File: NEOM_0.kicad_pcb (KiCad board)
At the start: 2 copper layers, 28 x 24 mm, 20 parts, among them U1 LM3940, U2 7_Pins_Header_PA0_PA6, U3 Reset Button, U4 STM32F070F6P6, U6 7_Pins_Header_PA7_PA14, U7 TPD4S012DRYR, U8 16Mhz, U9 USB_Micro_B

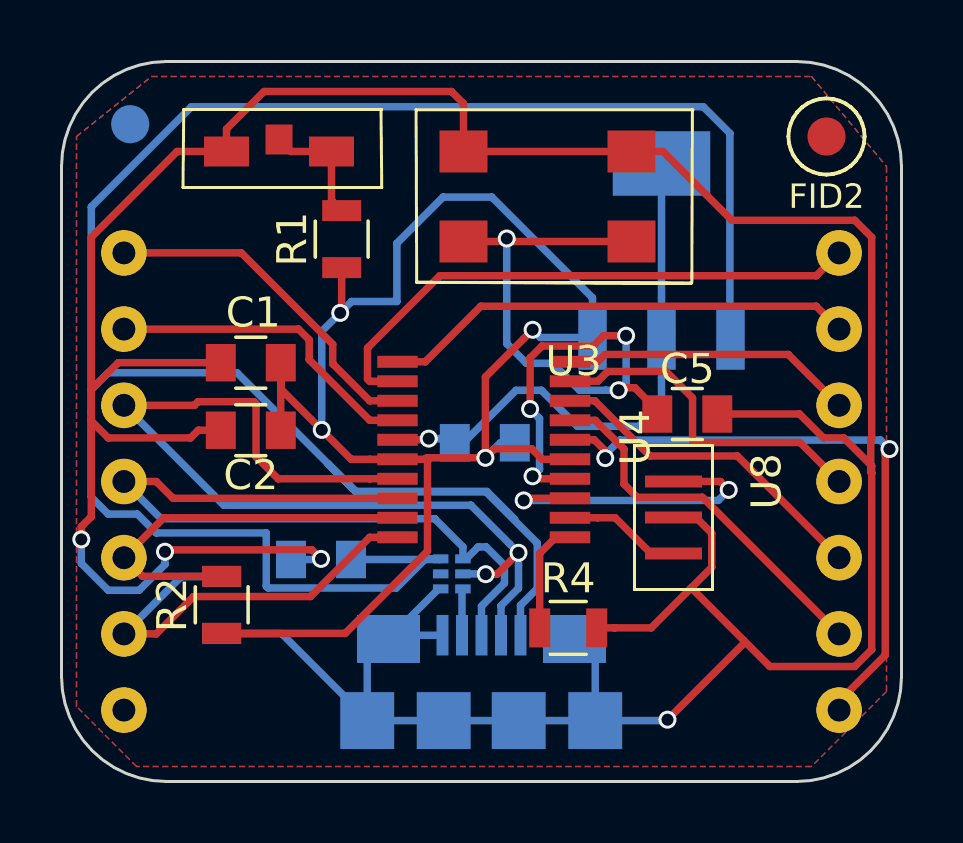
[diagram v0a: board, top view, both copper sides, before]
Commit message: Updated the PCB unconnected GND pad..
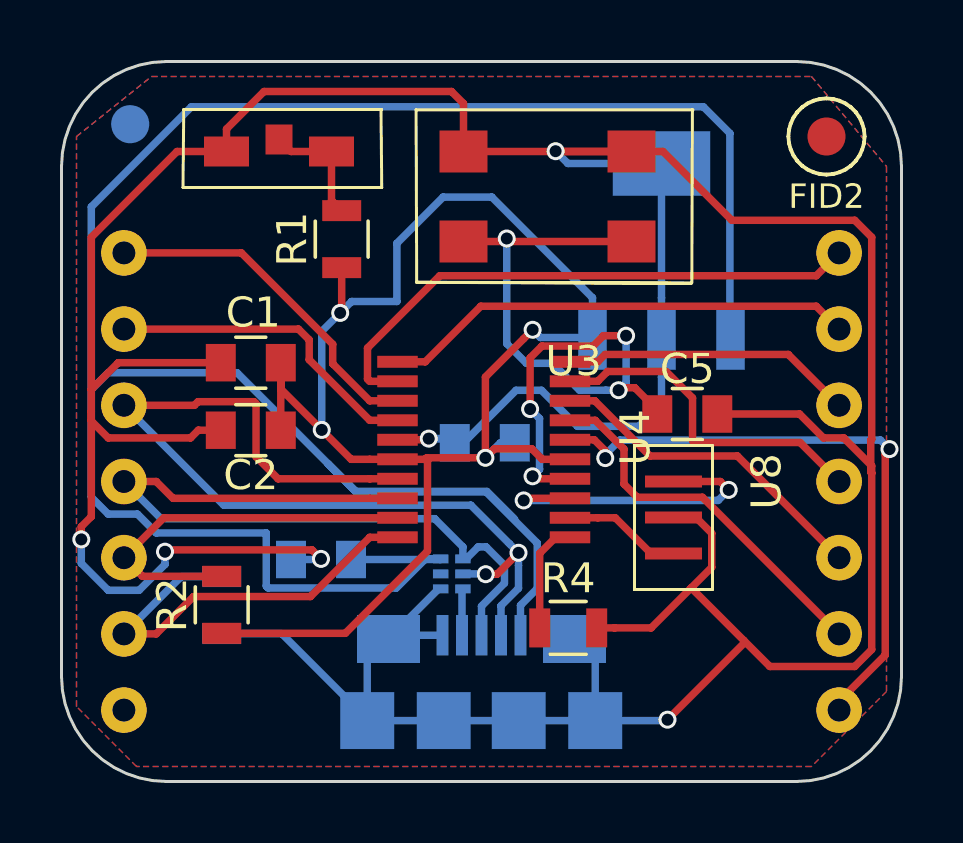
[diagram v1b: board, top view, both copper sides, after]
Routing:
- net GND: track 146.2 -> 152.5 mm, vias 5 -> 6
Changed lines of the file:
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@@
   (general
     (links 59)
-    (no_connects 1)
+    (no_connects 0)
     (area 105.875 87.31474 141.975 116.015)
     (thickness 1.6)
     (drawings 9)
-    (tracks 319)
+    (tracks 324)
     (zones 0)
     (modules 20)
@@
     (visible_elements FFFFFF7F)
     (pcbplotparams
-      (layerselection 0x00030_80000001)
+      (layerselection 0x010fc_80000001)
       (usegerberextensions false)
       (excludeedgelayer true)
@@
       (outputformat 1)
       (mirror false)
-      (drillshape 1)
+      (drillshape 0)
       (scaleselection 1)
-      (outputdirectory ""))
+      (outputdirectory Gerbers/))
   )
   (net 0 "")
@@
   (segment (start 117.31 99.04) (end 117.31 99.915) (width 0.25) (layer F.Cu) (net 1))
   (segment (start 120.275 102.26) (end 121.2 102.26) (width 0.25) (layer F.Cu) (net 1))
+  (segment (start 130 92.4) (end 126.88 92.4) (width 0.25) (layer B.Cu) (net 2))
+  (segment (start 126.47 92) (end 129 92) (width 0.25) (layer F.Cu) (net 2))
+  (segment (start 126.47 91.99) (end 126.47 92) (width 0.25) (layer F.Cu) (net 2))
+  (via (at 126.47 91.99) (size 0.6) (drill 0.4) (layers F.Cu B.Cu) (net 2))
+  (segment (start 126.88 92.4) (end 126.47 91.99) (width 0.25) (layer B.Cu) (net 2))
   (segment (start 127.200267 101.159988) (end 129.253602 101.159988) (width 0.25) (layer B.Cu) (net 2))
   (segment (start 130 100.41359) (end 130 99.525) (width 0.25) (layer B.Cu) (net 2))
@@
   (segment (start 123.539998 101.57) (end 125.1499 99.960098) (width 0.25) (layer B.Cu) (net 2))
   (segment (start 136.974998 101.619998) (end 136.974998 102.687997) (width 0.25) (layer F.Cu) (net 2))
+  (segment (start 132.342999 94.292999) (end 136.441761 94.292999) (width 0.25) (layer F.Cu) (net 2))
+  (segment (start 137.007001 94.858239) (end 137.007001 101.587995) (width 0.25) (layer F.Cu) (net 2))
+  (segment (start 129 92) (end 130.05 92) (width 0.25) (layer F.Cu) (net 2))
+  (segment (start 130.05 92) (end 132.342999 94.292999) (width 0.25) (layer F.Cu) (net 2))
+  (segment (start 136.974998 102.687997) (end 137.007001 102.72) (width 0.25) (layer F.Cu) (net 2))
+  (segment (start 136.441761 94.292999) (end 137.007001 94.858239) (width 0.25) (layer F.Cu) (net 2))
   (segment (start 137.007001 101.587995) (end 136.974998 101.619998) (width 0.25) (layer F.Cu) (net 2))
-  (segment (start 136.441761 94.292999) (end 137.007001 94.858239) (width 0.25) (layer F.Cu) (net 2))
-  (segment (start 136.974998 102.687997) (end 137.007001 102.72) (width 0.25) (layer F.Cu) (net 2))
-  (segment (start 130.05 92) (end 132.342999 94.292999) (width 0.25) (layer F.Cu) (net 2))
-  (segment (start 129 92) (end 130.05 92) (width 0.25) (layer F.Cu) (net 2))
-  (segment (start 137.007001 94.858239) (end 137.007001 101.587995) (width 0.25) (layer F.Cu) (net 2))
-  (segment (start 132.342999 94.292999) (end 136.441761 94.292999) (width 0.25) (layer F.Cu) (net 2))
   (segment (start 110.992999 99.938239) (end 110.992999 100.65) (width 0.25) (layer F.Cu) (net 2))
   (segment (start 110.992999 100.65) (end 110.992999 100.981761) (width 0.25) (layer F.Cu) (net 2))

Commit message: Added BAT pin for external battery board..
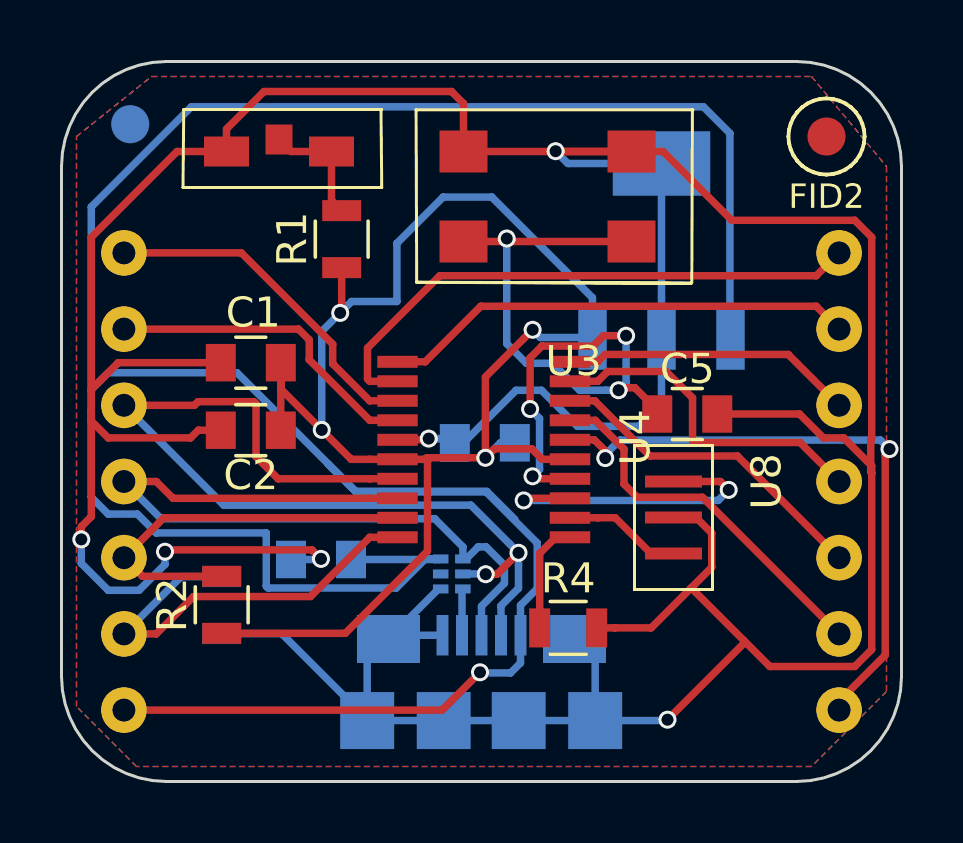
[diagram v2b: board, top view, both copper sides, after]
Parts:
- D1: value PWR -> LED
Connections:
- U6 pad 7: Net-(U6-Pad7) -> /VBUS
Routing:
- net /VBUS: track 84.6 -> 99.4 mm, vias 0 -> 1

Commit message: Updated PCB with logo..
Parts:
- added G***: LOGO, Graphics:logo, B.Cu at (116.2, 95.7)

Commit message: Updated PCB with logo..
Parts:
- moved G*** 2.29 mm to (116.2, 98.0)
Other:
- board text added: "Proudly Designed in"
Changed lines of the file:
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@@
 (kicad_pcb (version 4) (host pcbnew 4.0.2-stable)
   (general
-    (links 0)
+    (links 60)
     (no_connects 0)
-    (area 105.875 87.31474 141.975 116.015)
+    (area 109.949999 88.949999 138.050001 113.050001)
     (thickness 1.6)
-    (drawings 9)
+    (drawings 10)
     (tracks 331)
     (zones 0)
@@
   )
   (module Graphics:logo (layer B.Cu)
-    (at 116.22 95.69 180)
+    (at 116.16 97.98 180)
     (fp_text reference G*** (at 0 0 180) (layer B.SilkS) hide
       (effects (font (thickness 0.3)) (justify mirror))
@@
       (xy -0.00539 1.56421) (xy 0 1.564641) (xy 0.02429 1.548197)) (layer B.SilkS) (width 0.01))
   )
-  (gr_text "NEOM 0" (at 119.5 92) (layer B.SilkS)
+  (gr_text "Proudly\nDesigned in" (at 119.42 94.52) (layer B.SilkS)
+    (effects (font (size 1 1) (thickness 0.1)) (justify mirror))
+  )
+  (gr_text "NEOM 0\n" (at 119.5 92) (layer B.SilkS)
     (effects (font (size 1.5 1.5) (thickness 0.3)) (justify mirror))
   )

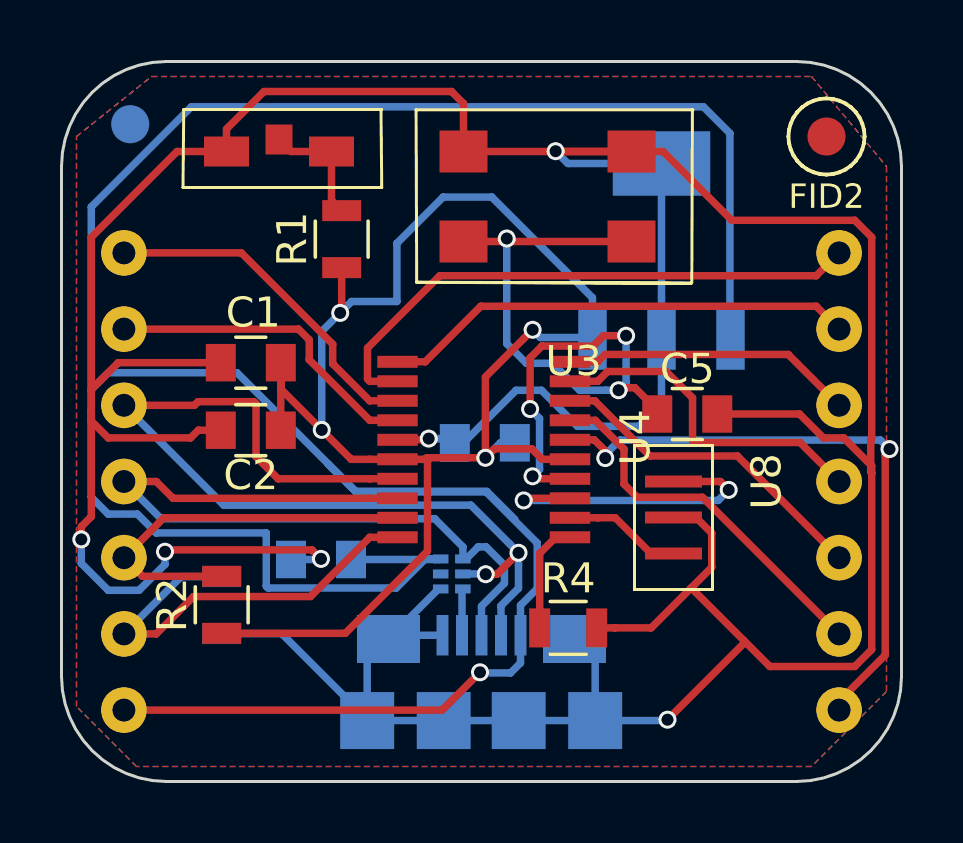
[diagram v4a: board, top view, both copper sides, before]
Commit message: Updated PCB with deminsion and Fab layer..
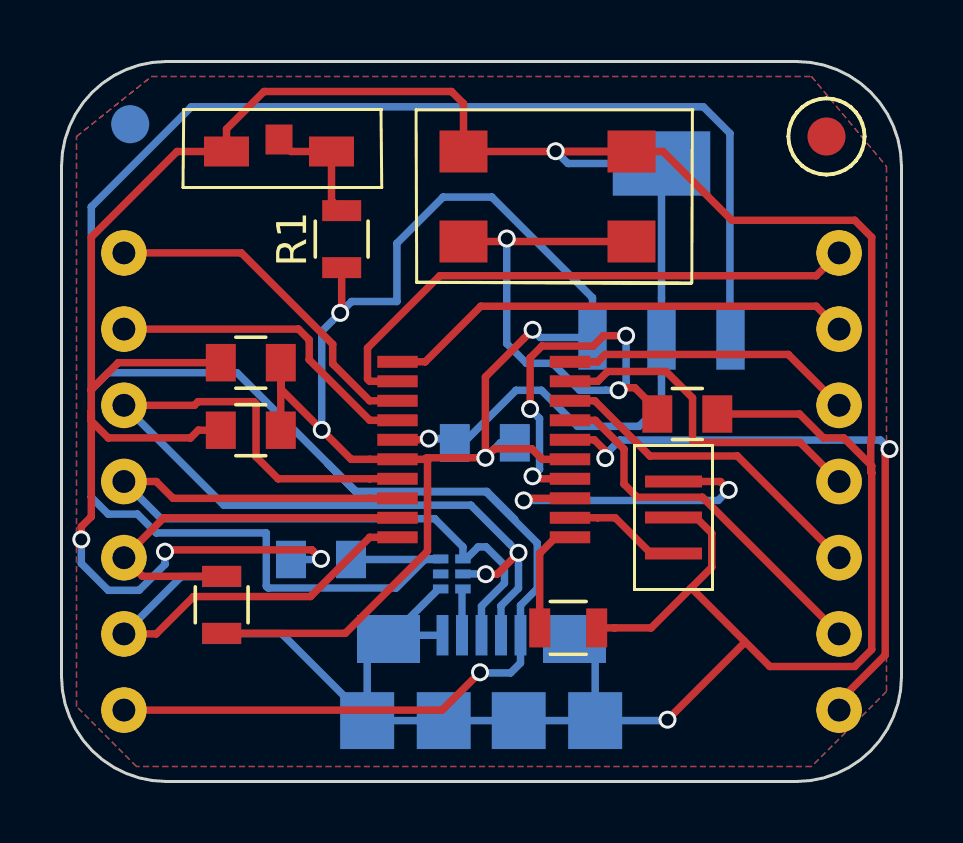
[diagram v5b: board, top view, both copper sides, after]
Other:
- rule pad_to_mask_clearance: 0 -> 0.05
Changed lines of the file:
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@@
     (links 60)
     (no_connects 0)
-    (area 109.949999 88.949999 138.050001 113.050001)
+    (area 105.875 87.31474 141.975 116.015)
     (thickness 1.6)
-    (drawings 10)
+    (drawings 12)
     (tracks 331)
     (zones 0)
@@
     (0 F.Cu signal)
     (31 B.Cu signal)
-    (32 B.Adhes user)
-    (33 F.Adhes user)
     (34 B.Paste user)
     (35 F.Paste user)
@@
     (39 F.Mask user)
     (40 Dwgs.User user)
-    (41 Cmts.User user)
-    (42 Eco1.User user)
-    (43 Eco2.User user)
     (44 Edge.Cuts user)
-    (45 Margin user)
-    (46 B.CrtYd user)
-    (47 F.CrtYd user)
     (48 B.Fab user)
     (49 F.Fab user)
@@
     (pad_size 1.5 1.5)
     (pad_drill 0.6)
-    (pad_to_mask_clearance 0)
+    (pad_to_mask_clearance 0.05)
     (aux_axis_origin 0 0)
     (visible_elements FFFFFF7F)
@@
     (tags "capacitor 0805")
     (attr smd)
-    (fp_text reference C1 (at -0.08 1.67 180) (layer F.SilkS)
+    (fp_text reference C1 (at -0.08 1.67 180) (layer F.Fab)
       (effects (font (size 1 1) (thickness 0.15)))
     )
@@
     (tags "capacitor 0805")
     (attr smd)
-    (fp_text reference C2 (at 0 -1.5 180) (layer F.SilkS)
+    (fp_text reference C2 (at 0 -1.5 180) (layer F.Fab)
       (effects (font (size 1 1) (thickness 0.15)))
     )
@@
     (tags "capacitor 0805")
     (attr smd)
-    (fp_text reference C3 (at 0 1.5) (layer B.SilkS)
+    (fp_text reference C3 (at 0 1.5) (layer B.Fab)
       (effects (font (size 1 1) (thickness 0.15)) (justify mirror))
     )
@@
     (tags "capacitor 0805")
     (attr smd)
-    (fp_text reference C4 (at 0 1.5) (layer B.SilkS)
+    (fp_text reference C4 (at 0 1.5) (layer B.Fab)
       (effects (font (size 1 1) (thickness 0.15)) (justify mirror))
     )
@@
     (tags "capacitor 0805")
     (attr smd)
-    (fp_text reference C5 (at 0 -1.5) (layer F.SilkS)
+    (fp_text reference C5 (at 0 -1.5) (layer F.Fab)
       (effects (font (size 1 1) (thickness 0.15)))
     )
@@
     (tags "DESCRIPTION: FOOTPRINT FOR FIDUCIAL MARKING FOR PCB ALIGNMENT INSIDE PNP AND OTHER MACHINES.")
     (attr smd)
-    (fp_text reference FID1 (at 0.0254 1.9812) (layer B.SilkS)
+    (fp_text reference FID1 (at 0.0254 1.9812) (layer B.Fab)
       (effects (font (size 0.8128 0.8128) (thickness 0.127)) (justify mirror))
     )
@@
     (tags "DESCRIPTION: FOOTPRINT FOR FIDUCIAL MARKING FOR PCB ALIGNMENT INSIDE PNP AND OTHER MACHINES.")
     (attr smd)
-    (fp_text reference FID2 (at 0 2) (layer F.SilkS)
+    (fp_text reference FID2 (at 0 2) (layer F.Fab)
       (effects (font (size 0.8128 0.8128) (thickness 0.127)))
     )
@@
     (tags "resistor 0805")
     (attr smd)
-    (fp_text reference R2 (at 0 -1.65 90) (layer F.SilkS)
+    (fp_text reference R2 (at 0 -1.65 90) (layer F.Fab)
       (effects (font (size 1 1) (thickness 0.15)))
     )
@@
     (tags "resistor 0805")
     (attr smd)
-    (fp_text reference R3 (at 0 1.65 270) (layer B.SilkS)
+    (fp_text reference R3 (at 0 1.65 270) (layer B.Fab)
       (effects (font (size 1 1) (thickness 0.15)) (justify mirror))
     )
@@
     (tags "resistor 0805")
     (attr smd)
-    (fp_text reference R4 (at 0 -1.65) (layer F.SilkS)
+    (fp_text reference R4 (at 0 -1.65) (layer F.Fab)
       (effects (font (size 1 1) (thickness 0.15)))
     )
@@
   (module Footprints:Tactile_Button (layer F.Cu)
     (at 129 98)
-    (fp_text reference U3 (at -1.93 0.99) (layer F.SilkS)
+    (fp_text reference U3 (at -1.93 0.99) (layer F.Fab)
       (effects (font (size 1 1) (thickness 0.15)))
     )
@@
     (descr NEOM_0)
     (tags STM32F070F6P6)
-    (fp_text reference U4 (at 6.84 -2.18 90) (layer F.SilkS)
+    (fp_text reference U4 (at 6.84 -2.18 90) (layer F.Fab)
       (effects (font (size 1 1) (thickness 0.15)))
     )
@@
   (module Footprints:16Mhz (layer F.Cu)
     (at 133 103 90)
-    (fp_text reference U8 (at 0 0.5 90) (layer F.SilkS)
+    (fp_text reference U8 (at 0 0.5 90) (layer F.Fab)
       (effects (font (size 1 1) (thickness 0.15)))
     )
@@
   (module Footprints2:MICRO_USB_B_Type (layer B.Cu)
     (at 124 111 180)
-    (fp_text reference U9 (at -0.06 -2.67 180) (layer B.SilkS) hide
+    (fp_text reference U9 (at -0.06 -2.67 180) (layer B.Fab) hide
       (effects (font (size 1 1) (thickness 0.15)) (justify mirror))
     )
@@
       (xy -0.00539 1.56421) (xy 0 1.564641) (xy 0.02429 1.548197)) (layer B.SilkS) (width 0.01))
   )
+  (dimension 24.06 (width 0.3) (layer Dwgs.User)
+    (gr_text "24.060 mm" (at 143.87 100.98 270) (layer Dwgs.User)
+      (effects (font (size 1.5 1.5) (thickness 0.3)))
+    )
+    (feature1 (pts (xy 133.77 113.01) (xy 145.22 113.01)))
+    (feature2 (pts (xy 133.77 88.95) (xy 145.22 88.95)))
+    (crossbar (pts (xy 142.52 88.95) (xy 142.52 113.01)))
+    (arrow1a (pts (xy 142.52 113.01) (xy 141.933579 111.883496)))
+    (arrow1b (pts (xy 142.52 113.01) (xy 143.106421 111.883496)))
+    (arrow2a (pts (xy 142.52 88.95) (xy 141.933579 90.076504)))
+    (arrow2b (pts (xy 142.52 88.95) (xy 143.106421 90.076504)))
+  )
+  (dimension 28.030045 (width 0.3) (layer Dwgs.User)
+    (gr_text "28.030 mm" (at 123.994279 86.124464 0.1022042789) (layer Dwgs.User)
+      (effects (font (size 1.5 1.5) (thickness 0.3)))
+    )
+    (feature1 (pts (xy 138.02 92.11) (xy 138.006871 84.749466)))
+    (feature2 (pts (xy 109.99 92.16) (xy 109.976871 84.799466)))
+    (crossbar (pts (xy 109.981687 87.499462) (xy 138.011687 87.449462)))
+    (arrow1a (pts (xy 138.011687 87.449462) (xy 136.886231 88.037891)))
+    (arrow1b (pts (xy 138.011687 87.449462) (xy 136.884139 86.865052)))
+    (arrow2a (pts (xy 109.981687 87.499462) (xy 111.109235 88.083872)))
+    (arrow2b (pts (xy 109.981687 87.499462) (xy 111.107143 86.911033)))
+  )
   (gr_text "Proudly\nDesigned in" (at 119.42 94.52) (layer B.SilkS)
     (effects (font (size 1 1) (thickness 0.1)) (justify mirror))
@@
   (segment (start 124.630001 101.71) (end 124.13 102.210001) (width 0.25) (layer B.Cu) (net 1))
   (segment (start 124.13 102.210001) (end 122.174999 102.210001) (width 0.25) (layer F.Cu) (net 1))
-  (via (at 124.13 102.210001) (size 0.6) (drill 0.4) (layers F.Cu B.Cu) (net 1))
+  (via (at 124.13 102.210001) (size 0.6) (drill 0.4) (layers F.Cu B.Cu) (net 1) (status 1000000))
   (segment (start 122.174999 102.210001) (end 122.125 102.26) (width 0.25) (layer F.Cu) (net 1))
   (segment (start 122.125 102.26) (end 121.2 102.26) (width 0.25) (layer F.Cu) (net 1))
